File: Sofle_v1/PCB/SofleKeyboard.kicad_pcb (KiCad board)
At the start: 2 copper layers, 137.2 x 109.2 mm, 87 parts, among them J1 LED, J2 4PIN, J3 OLED, P1 i2c_pin, P2 i2c_pin, SW1 SW_PUSH, SW10 SW_PUSH, SW11 SW_PUSH, SW12 SW_PUSH, SW13 SW_PUSH, SW14 SW_PUSH, SW15 SW_PUSH, SW16 SW_PUSH, SW17 SW_PUSH, SW18 SW_PUSH, SW19 SW_PUSH, SW2 SW_PUSH, SW20 SW_PUSH, SW21 SW_PUSH, SW22 SW_PUSH, SW23 SW_PUSH, SW24 SW_PUSH, SW25 Rotary_Encoder_Switch, SW26 SW_PUSH, SW27 SW_PUSH, SW28 SW_PUSH, SW29 SW_PUSH, SW3 SW_PUSH, SW30 SW_PUSH, SW4 SW_PUSH, SW5 SW_PUSH, SW6 SW_PUSH, SW7 SW_PUSH, SW8 SW_PUSH, SW9 SW_PUSH, U1 ProMicro

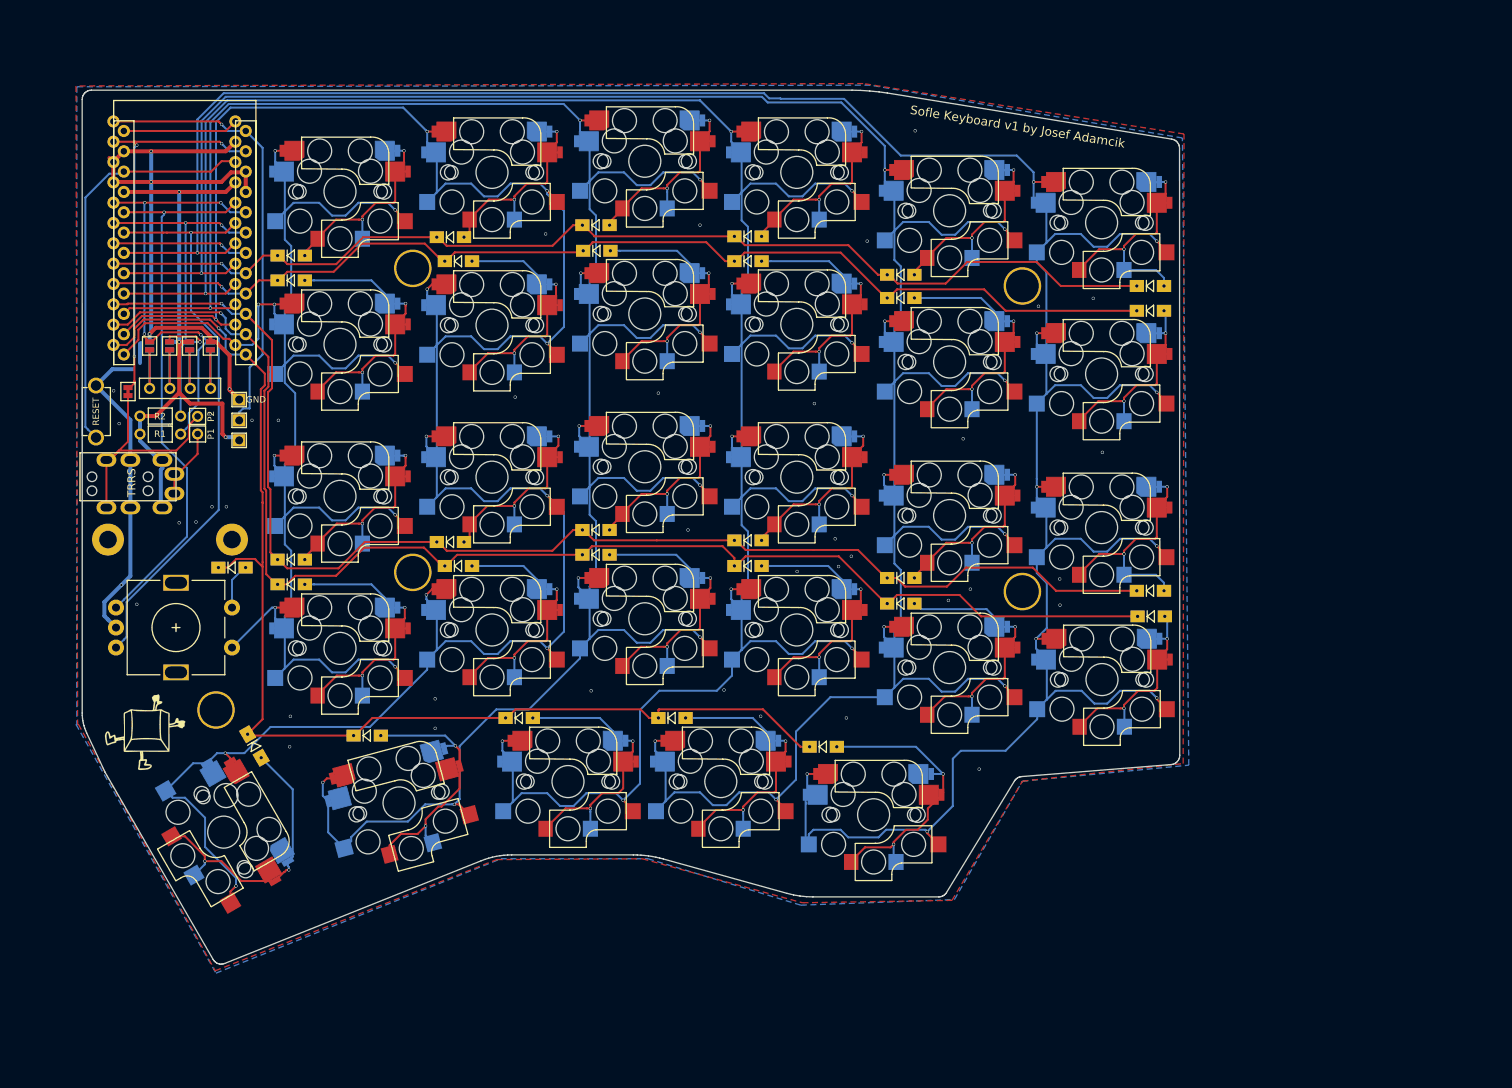
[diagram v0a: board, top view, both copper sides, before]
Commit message: Added Column 6
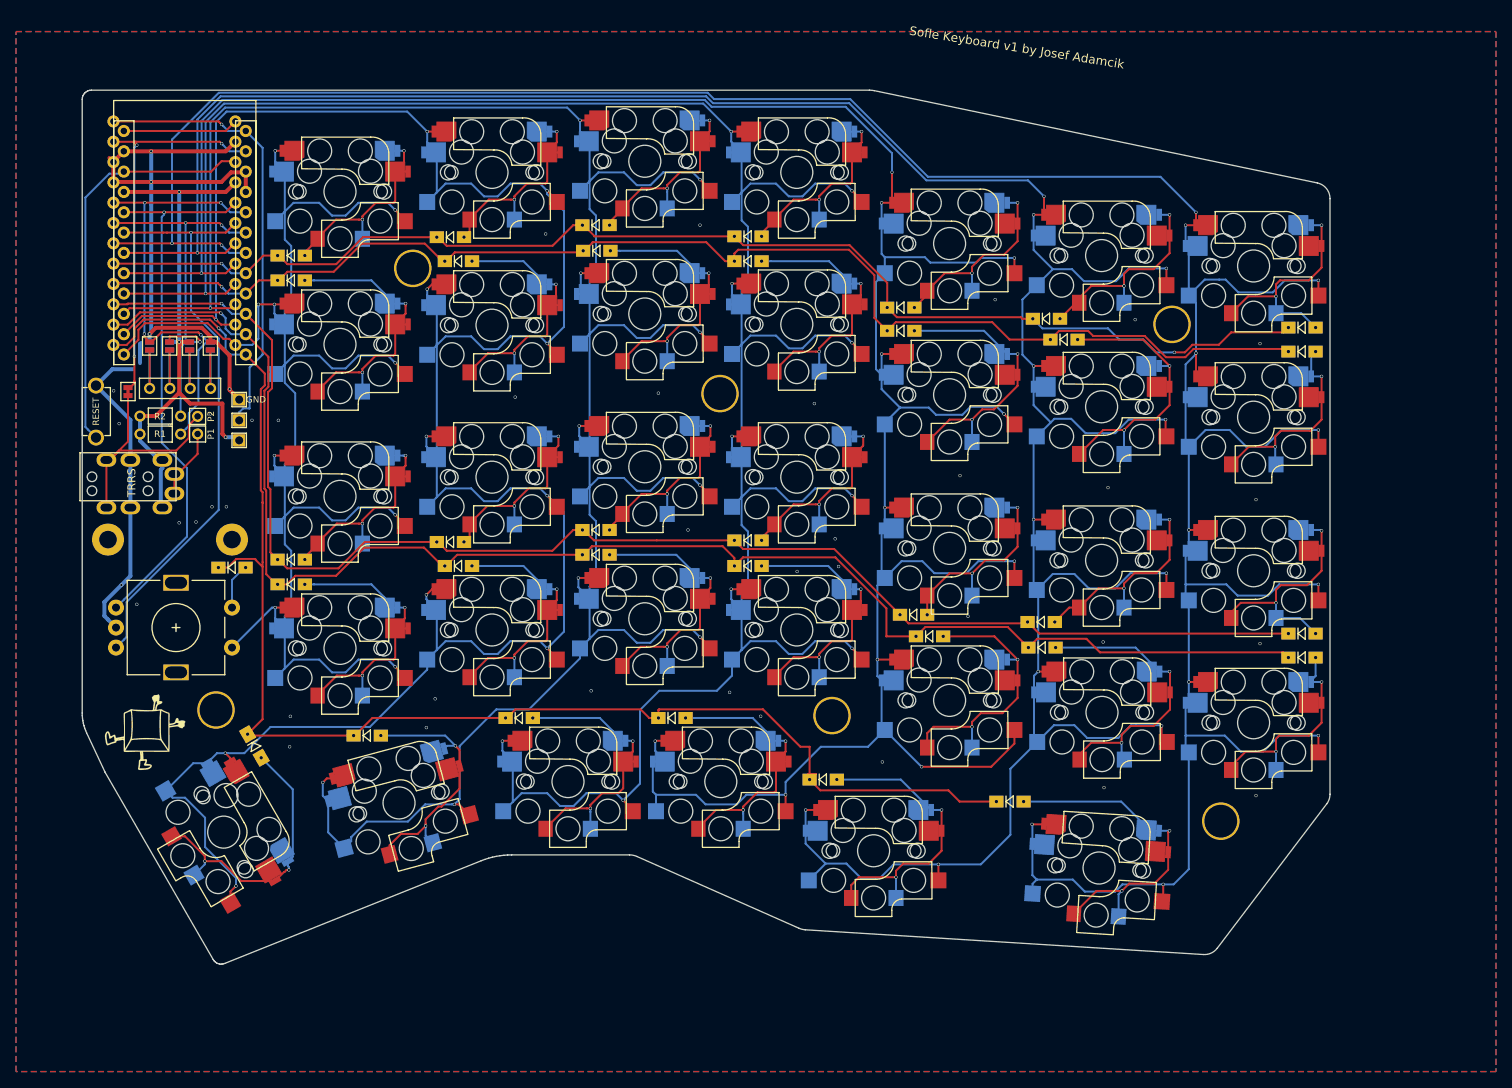
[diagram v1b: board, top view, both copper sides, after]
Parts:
- added D31: D, SofleKeyboard-footprint:Diode_SOD123, F.Cu at (240.8, 67.0)
- added D32: D, SofleKeyboard-footprint:Diode_SOD123, F.Cu at (240.8, 70.0)
- added D33: D, SofleKeyboard-footprint:Diode_SOD123, F.Cu at (240.8, 105.2)
- added D34: D, SofleKeyboard-footprint:Diode_SOD123, F.Cu at (240.8, 108.2)
- added D35: D, SofleKeyboard-footprint:Diode_SOD123, F.Cu at (204.2, 126.2)
- added SW31: SW_PUSH, SofleKeyboard-footprint:CherryMX_KailhLowProfile_Hotswap, F.Cu at (234.7, 59.3)
- added SW32: SW_PUSH, SofleKeyboard-footprint:CherryMX_KailhLowProfile_Hotswap, F.Cu at (234.7, 78.2)
- added SW33: SW_PUSH, SofleKeyboard-footprint:CherryMX_KailhLowProfile_Hotswap, F.Cu at (234.7, 97.4)
- added SW34: SW_PUSH, SofleKeyboard-footprint:CherryMX_KailhLowProfile_Hotswap, F.Cu at (234.7, 116.4)
- added SW35: SW_PUSH, SofleKeyboard-footprint:CherryMX_KailhLowProfile_Hotswap, F.Cu at (215.4, 134.6)
- added TH8: HOLE, SofleKeyboard-footprint:HOLE_M2_TH, F.Cu at (182.0, 115.5)
- moved TH5 44.4 mm to (168.0, 75.2)
- moved TH6 37.9 mm to (230.6, 128.7)
- moved TH4 19.3 mm to (224.5, 66.6)
- moved D24 14.2 mm to (208.2, 107.0)
- moved D18 14.2 mm to (208.2, 103.8)
- moved D6 13.6 mm to (208.8, 65.9)
- moved D12 11.4 mm to (211.0, 68.5)
- moved D23 5.46 mm to (194.2, 105.6)
- moved D17 4.87 mm to (192.2, 102.9)
- moved SW30 4.50 mm to (187.2, 132.4)
- moved D11 4.10 mm to (190.6, 67.4)
- moved SW11 4.10 mm to (196.7, 75.4)
- moved SW12 4.10 mm to (215.7, 76.9)
- moved D5 4.10 mm to (190.6, 64.5)
- moved SW5 4.10 mm to (196.7, 56.5)
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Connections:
- net SW25A renamed col5
- net SW25B renamed row4-sw25
- U1 pad 24: Net-(U1-Pad24) -> unconnected-(U1-RAW-Pad24)
- U1 pad 7: Net-(U1-Pad7) -> col6
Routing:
- net col6: track 0.00 -> 371.5 mm, vias 0 -> 13
- net Net-(D35-A): track 0.00 -> 42.1 mm, vias 0 -> 2
- net row4: track 152.5 -> 182.0 mm
- net Net-(D33-A): track 0.00 -> 29.1 mm, vias 0 -> 2
- net Net-(D31-A): track 0.00 -> 28.9 mm, vias 0 -> 2
- net Net-(D34-A): track 0.00 -> 27.0 mm, vias 0 -> 2
- net row1: track 138.3 -> 165.1 mm
- net Net-(D32-A): track 0.00 -> 26.7 mm, vias 0 -> 2
- net row3: track 170.1 -> 194.0 mm
- net row0: track 138.2 -> 161.4 mm, vias 1 -> 2
- net row2: track 165.8 -> 185.1 mm
- net col1: track 350.6 -> 333.0 mm, vias 11 -> 12
- net Net-(U1-Pad7): track 17.0 -> 0.00 mm, vias 1 -> 0
- net Net-(U1-Pad24): track 14.4 -> 0.00 mm
- net (no net): track 0.00 -> 14.4 mm
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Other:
- board size 137.2 x 109.2 mm -> 156 x 109.2 mm
- net class Default removed
- net class GND removed
- net class VCC removed
